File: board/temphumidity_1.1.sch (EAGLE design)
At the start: 33 parts, among them J1 10118192-0001LF, J2 B2B-PH-K-S(LF)(SN), Q1 MMBT2222A, Q2 MMBT2222A, U1 ENS210-LQFM, U2 ESP-WROOM-02, U3 FT231XS-U

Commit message: More revisions on 1.1, added pictures for Readme
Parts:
- removed JP2: (no value), pinhead:PINHD-1X3
- added R15: 4.7k, rcl:R-US_R0805
- added R16: 10k, rcl:R-US_R0805
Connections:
- net 3V3: no longer JP2.1
- net ADC: now also R15.2, R16.1; no longer JP2.2
- net GND: now also R16.2; no longer JP2.3
- net VBAT: now also R15.1
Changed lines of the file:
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@@
 <part name="R9" library="rcl" library_urn="urn:adsk.eagle:library:334" deviceset="R-US_" device="R0805" package3d_urn="urn:adsk.eagle:package:23553/2" value="10k"/>
 <part name="R10" library="rcl" library_urn="urn:adsk.eagle:library:334" deviceset="R-US_" device="R0805" package3d_urn="urn:adsk.eagle:package:23553/2" value="100k"/>
-<part name="JP2" library="pinhead" library_urn="urn:adsk.eagle:library:325" deviceset="PINHD-1X3" device="" package3d_urn="urn:adsk.eagle:package:22458/2"/>
 <part name="J2" library="B2B-PH-K-S_LF__SN_" deviceset="B2B-PH-K-S(LF)(SN)" device=""/>
 <part name="U$2" library="SON50P300X300X80-11N" deviceset="RT9532GQW" device=""/>
@@
 <part name="R14" library="rcl" library_urn="urn:adsk.eagle:library:334" deviceset="R-US_" device="R0805" package3d_urn="urn:adsk.eagle:package:23553/2" value="27"/>
 <part name="VR1" library="AP7366-33W5-7" deviceset="AP7366-33W5-7" device=""/>
+<part name="R15" library="rcl" library_urn="urn:adsk.eagle:library:334" deviceset="R-US_" device="R0805" package3d_urn="urn:adsk.eagle:package:23553/2" value="4.7k"/>
+<part name="R16" library="rcl" library_urn="urn:adsk.eagle:library:334" deviceset="R-US_" device="R0805" package3d_urn="urn:adsk.eagle:package:23553/2" value="10k"/>
 </parts>
 <sheets>
@@
 <attribute name="VALUE" x="24.13" y="-41.402" size="1.778" layer="96"/>
 </instance>
-<instance part="JP2" gate="A" x="-22.86" y="35.56" smashed="yes">
-<attribute name="NAME" x="-29.21" y="41.275" size="1.778" layer="95"/>
-<attribute name="VALUE" x="-29.21" y="27.94" size="1.778" layer="96"/>
-</instance>
 <instance part="VR1" gate="G$1" x="-25.4" y="-50.8" smashed="yes">
 <attribute name="NAME" x="-33.02" y="-44.45" size="2.54" layer="95"/>
 <attribute name="VALUE" x="-33.02" y="-57.15" size="2.54" layer="96" align="top-left"/>
+</instance>
+<instance part="R15" gate="G$1" x="104.14" y="-33.02" smashed="yes" rot="R270">
+<attribute name="NAME" x="105.6386" y="-29.21" size="1.778" layer="95" rot="R270"/>
+<attribute name="VALUE" x="100.838" y="-29.21" size="1.778" layer="96" rot="R270"/>
+</instance>
+<instance part="R16" gate="G$1" x="104.14" y="-48.26" smashed="yes" rot="R270">
+<attribute name="NAME" x="105.6386" y="-44.45" size="1.778" layer="95" rot="R270"/>
+<attribute name="VALUE" x="100.838" y="-44.45" size="1.778" layer="96" rot="R270"/>
 </instance>
 </instances>
@@
 </segment>
 <segment>
-<pinref part="JP2" gate="A" pin="3"/>
-<wire x1="-25.4" y1="33.02" x2="-33.02" y2="33.02" width="0.1524" layer="91"/>
-<label x="-33.02" y="33.02" size="1.778" layer="95" rot="R180"/>
-</segment>
-<segment>
 <pinref part="U2" gate="G$1" pin="GND"/>
 <wire x1="71.12" y1="-63.5" x2="73.66" y2="-63.5" width="0.1524" layer="91"/>
 <label x="73.66" y="-63.5" size="1.778" layer="95"/>
+</segment>
+<segment>
+<pinref part="R16" gate="G$1" pin="2"/>
+<wire x1="104.14" y1="-53.34" x2="104.14" y2="-55.88" width="0.1524" layer="91"/>
+<label x="104.14" y="-55.88" size="1.778" layer="95"/>
 </segment>
 </net>
@@
 <label x="20.32" y="-38.1" size="1.778" layer="95" rot="R180"/>
 </segment>
-<segment>
-<pinref part="JP2" gate="A" pin="1"/>
-<wire x1="-25.4" y1="38.1" x2="-33.02" y2="38.1" width="0.1524" layer="91"/>
-<label x="-33.02" y="38.1" size="1.778" layer="95" rot="R180"/>
-</segment>
 </net>
 <net name="SCL" class="0">
@@
 <wire x1="-58.42" y1="-43.18" x2="-58.42" y2="-40.64" width="0.1524" layer="91"/>
 <label x="-58.42" y="-40.64" size="1.778" layer="95"/>
+</segment>
+<segment>
+<pinref part="R15" gate="G$1" pin="1"/>
+<wire x1="104.14" y1="-27.94" x2="104.14" y2="-25.4" width="0.1524" layer="91"/>
+<label x="104.14" y="-25.4" size="1.778" layer="95"/>
 </segment>
 </net>
@@
 <segment>
 <pinref part="U2" gate="G$1" pin="TOUT"/>
-<wire x1="71.12" y1="-40.64" x2="73.66" y2="-40.64" width="0.1524" layer="91"/>
 <label x="73.66" y="-40.64" size="1.778" layer="95"/>
-</segment>
-<segment>
-<pinref part="JP2" gate="A" pin="2"/>
-<wire x1="-25.4" y1="35.56" x2="-33.02" y2="35.56" width="0.1524" layer="91"/>
-<label x="-33.02" y="35.56" size="1.778" layer="95" rot="R180"/>
-</segment>
-</net>
+<wire x1="71.12" y1="-40.64" x2="104.14" y2="-40.64" width="0.1524" layer="91"/>
+<pinref part="R15" gate="G$1" pin="2"/>
+<wire x1="104.14" y1="-40.64" x2="104.14" y2="-38.1" width="0.1524" layer="91"/>
+<pinref part="R16" gate="G$1" pin="1"/>
+<wire x1="104.14" y1="-40.64" x2="104.14" y2="-43.18" width="0.1524" layer="91"/>
+<junction x="104.14" y="-40.64"/>
+</segment>
+</net>

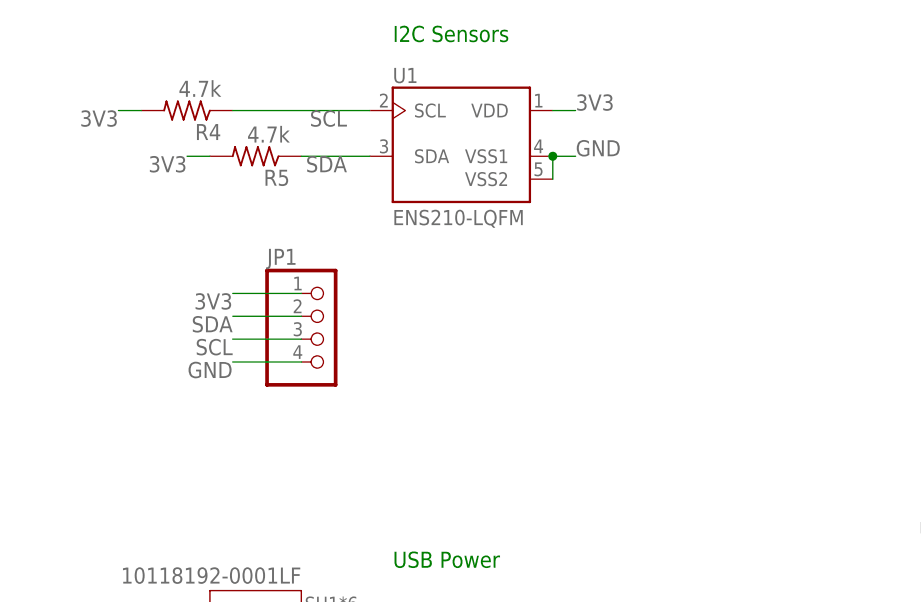
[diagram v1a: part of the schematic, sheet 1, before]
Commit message: Wrote spring application to make use of sql database
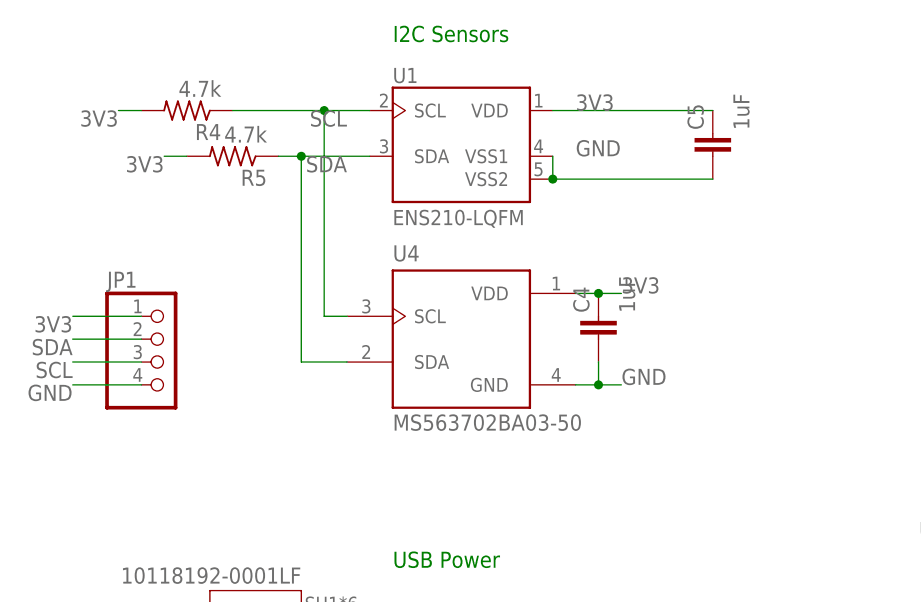
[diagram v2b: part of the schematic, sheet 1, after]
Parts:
- added C4, C5: 1uF, rcl:C-EUC0805
- added U4: MS563702BA03-50, MS563702BA03-50:MS563702BA03-50
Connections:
- net 3V3: now also C4.1, C5.1, U4.VDD
- net GND: now also C4.2, C5.2, U4.GND
- net SCL: now also U4.SCL
- net SDA: now also U4.SDA
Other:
- moved on the sheet: JP1, R5
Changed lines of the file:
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@@
 <part name="R15" library="rcl" library_urn="urn:adsk.eagle:library:334" deviceset="R-US_" device="R0805" package3d_urn="urn:adsk.eagle:package:23553/2" value="4.7k"/>
 <part name="R16" library="rcl" library_urn="urn:adsk.eagle:library:334" deviceset="R-US_" device="R0805" package3d_urn="urn:adsk.eagle:package:23553/2" value="10k"/>
+<part name="U4" library="MS563702BA03-50" deviceset="MS563702BA03-50" device=""/>
+<part name="C4" library="rcl" library_urn="urn:adsk.eagle:library:334" deviceset="C-EU" device="C0805" package3d_urn="urn:adsk.eagle:package:23617/2" value="1uF"/>
+<part name="C5" library="rcl" library_urn="urn:adsk.eagle:library:334" deviceset="C-EU" device="C0805" package3d_urn="urn:adsk.eagle:package:23617/2" value="1uF"/>
 </parts>
 <sheets>
@@
 <attribute name="VALUE" x="-54.61" y="61.722" size="1.778" layer="96" rot="R180"/>
 </instance>
-<instance part="R5" gate="G$1" x="-50.8" y="53.34" smashed="yes" rot="R180">
-<attribute name="NAME" x="-46.99" y="51.8414" size="1.778" layer="95" rot="R180"/>
-<attribute name="VALUE" x="-46.99" y="56.642" size="1.778" layer="96" rot="R180"/>
-</instance>
-<instance part="JP1" gate="A" x="-43.18" y="33.02" smashed="yes">
-<attribute name="NAME" x="-49.53" y="41.275" size="1.778" layer="95"/>
-<attribute name="VALUE" x="-49.53" y="25.4" size="1.778" layer="96"/>
+<instance part="R5" gate="G$1" x="-53.34" y="53.34" smashed="yes" rot="R180">
+<attribute name="NAME" x="-49.53" y="51.8414" size="1.778" layer="95" rot="R180"/>
+<attribute name="VALUE" x="-49.53" y="56.642" size="1.778" layer="96" rot="R180"/>
+</instance>
+<instance part="JP1" gate="A" x="-60.96" y="30.48" smashed="yes">
+<attribute name="NAME" x="-67.31" y="38.735" size="1.778" layer="95"/>
+<attribute name="VALUE" x="-67.31" y="22.86" size="1.778" layer="96"/>
 </instance>
 <instance part="U3" gate="G$1" x="53.34" y="7.62" smashed="yes">
@@
 <attribute name="NAME" x="105.6386" y="-44.45" size="1.778" layer="95" rot="R270"/>
 <attribute name="VALUE" x="100.838" y="-44.45" size="1.778" layer="96" rot="R270"/>
+</instance>
+<instance part="U4" gate="G$1" x="-27.94" y="33.02" smashed="yes">
+<attribute name="NAME" x="-35.566640625" y="41.66351875" size="1.77955" layer="95"/>
+<attribute name="VALUE" x="-35.562240625" y="22.857" size="1.77851875" layer="96"/>
+</instance>
+<instance part="C4" gate="G$1" x="-12.7" y="35.56" smashed="yes">
+<attribute name="NAME" x="-13.716" y="35.941" size="1.778" layer="95" rot="R90"/>
+<attribute name="VALUE" x="-8.636" y="35.941" size="1.778" layer="96" rot="R90"/>
+</instance>
+<instance part="C5" gate="G$1" x="0" y="55.88" smashed="yes">
+<attribute name="NAME" x="-1.016" y="56.261" size="1.778" layer="95" rot="R90"/>
+<attribute name="VALUE" x="4.064" y="56.261" size="1.778" layer="96" rot="R90"/>
 </instance>
 </instances>
@@
 </segment>
 <segment>
+<pinref part="C5" gate="G$1" pin="2"/>
+<wire x1="0" y1="50.8" x2="-17.78" y2="50.8" width="0.1524" layer="91"/>
+<pinref part="U1" gate="G$1" pin="VSS2"/>
 <pinref part="U1" gate="G$1" pin="VSS1"/>
-<pinref part="U1" gate="G$1" pin="VSS2"/>
 <wire x1="-17.78" y1="53.34" x2="-17.78" y2="50.8" width="0.1524" layer="91"/>
-<wire x1="-17.78" y1="53.34" x2="-15.24" y2="53.34" width="0.1524" layer="91"/>
-<junction x="-17.78" y="53.34"/>
 <label x="-15.24" y="53.34" size="1.778" layer="95"/>
+<junction x="-17.78" y="50.8"/>
 </segment>
 <segment>
 <pinref part="JP1" gate="A" pin="4"/>
-<wire x1="-45.72" y1="30.48" x2="-53.34" y2="30.48" width="0.1524" layer="91"/>
-<label x="-53.34" y="30.48" size="1.778" layer="95" rot="R180"/>
+<wire x1="-63.5" y1="27.94" x2="-71.12" y2="27.94" width="0.1524" layer="91"/>
+<label x="-71.12" y="27.94" size="1.778" layer="95" rot="R180"/>
 </segment>
 <segment>
@@
 <wire x1="104.14" y1="-53.34" x2="104.14" y2="-55.88" width="0.1524" layer="91"/>
 <label x="104.14" y="-55.88" size="1.778" layer="95"/>
+</segment>
+<segment>
+<pinref part="U4" gate="G$1" pin="GND"/>
+<wire x1="-15.24" y1="27.94" x2="-12.7" y2="27.94" width="0.1524" layer="91"/>
+<label x="-10.16" y="27.94" size="1.778" layer="95"/>
+<pinref part="C4" gate="G$1" pin="2"/>
+<wire x1="-12.7" y1="27.94" x2="-10.16" y2="27.94" width="0.1524" layer="91"/>
+<wire x1="-12.7" y1="30.48" x2="-12.7" y2="27.94" width="0.1524" layer="91"/>
+<junction x="-12.7" y="27.94"/>
 </segment>
 </net>
@@
 <segment>
 <pinref part="U1" gate="G$1" pin="VDD"/>
-<wire x1="-17.78" y1="58.42" x2="-15.24" y2="58.42" width="0.1524" layer="91"/>
 <label x="-15.24" y="58.42" size="1.778" layer="95"/>
+<pinref part="C5" gate="G$1" pin="1"/>
+<wire x1="-17.78" y1="58.42" x2="0" y2="58.42" width="0.1524" layer="91"/>
 </segment>
 <segment>
 <pinref part="R5" gate="G$1" pin="2"/>
-<wire x1="-55.88" y1="53.34" x2="-58.42" y2="53.34" width="0.1524" layer="91"/>
-<label x="-58.42" y="53.34" size="1.778" layer="95" rot="R180"/>
+<wire x1="-58.42" y1="53.34" x2="-60.96" y2="53.34" width="0.1524" layer="91"/>
+<label x="-60.96" y="53.34" size="1.778" layer="95" rot="R180"/>
 </segment>
 <segment>
@@
 <segment>
 <pinref part="JP1" gate="A" pin="1"/>
-<wire x1="-45.72" y1="38.1" x2="-53.34" y2="38.1" width="0.1524" layer="91"/>
-<label x="-53.34" y="38.1" size="1.778" layer="95" rot="R180"/>
+<wire x1="-63.5" y1="35.56" x2="-71.12" y2="35.56" width="0.1524" layer="91"/>
+<label x="-71.12" y="35.56" size="1.778" layer="95" rot="R180"/>
 </segment>
 <segment>
@@
 <label x="20.32" y="-38.1" size="1.778" layer="95" rot="R180"/>
 </segment>
+<segment>
+<pinref part="U4" gate="G$1" pin="VDD"/>
+<wire x1="-15.24" y1="38.1" x2="-12.7" y2="38.1" width="0.1524" layer="91"/>
+<label x="-10.16" y="38.1" size="1.778" layer="95"/>
+<pinref part="C4" gate="G$1" pin="1"/>
+<wire x1="-12.7" y1="38.1" x2="-10.16" y2="38.1" width="0.1524" layer="91"/>
+<junction x="-12.7" y="38.1"/>
+</segment>
 </net>
 <net name="SCL" class="0">
@@
 <label x="-40.64" y="58.42" size="1.778" layer="95" rot="R180"/>
 <pinref part="R4" gate="G$1" pin="1"/>
-<wire x1="-38.1" y1="58.42" x2="-53.34" y2="58.42" width="0.1524" layer="91"/>
+<wire x1="-38.1" y1="58.42" x2="-43.18" y2="58.42" width="0.1524" layer="91"/>
+<pinref part="U4" gate="G$1" pin="SCL"/>
+<wire x1="-43.18" y1="58.42" x2="-53.34" y2="58.42" width="0.1524" layer="91"/>
+<wire x1="-40.64" y1="35.56" x2="-43.18" y2="35.56" width="0.1524" layer="91"/>
+<wire x1="-43.18" y1="35.56" x2="-43.18" y2="58.42" width="0.1524" layer="91"/>
+<junction x="-43.18" y="58.42"/>
 </segment>
 <segment>
 <pinref part="JP1" gate="A" pin="3"/>
-<wire x1="-45.72" y1="33.02" x2="-53.34" y2="33.02" width="0.1524" layer="91"/>
-<label x="-53.34" y="33.02" size="1.778" layer="95" rot="R180"/>
+<wire x1="-63.5" y1="30.48" x2="-71.12" y2="30.48" width="0.1524" layer="91"/>
+<label x="-71.12" y="30.48" size="1.778" layer="95" rot="R180"/>
 </segment>
 </net>
@@
 <pinref part="R5" gate="G$1" pin="1"/>
 <wire x1="-38.1" y1="53.34" x2="-45.72" y2="53.34" width="0.1524" layer="91"/>
+<pinref part="U4" gate="G$1" pin="SDA"/>
+<wire x1="-45.72" y1="53.34" x2="-48.26" y2="53.34" width="0.1524" layer="91"/>
+<wire x1="-40.64" y1="30.48" x2="-45.72" y2="30.48" width="0.1524" layer="91"/>
+<wire x1="-45.72" y1="30.48" x2="-45.72" y2="53.34" width="0.1524" layer="91"/>
+<junction x="-45.72" y="53.34"/>
 </segment>
 <segment>
 <pinref part="JP1" gate="A" pin="2"/>
-<wire x1="-45.72" y1="35.56" x2="-53.34" y2="35.56" width="0.1524" layer="91"/>
-<label x="-53.34" y="35.56" size="1.778" layer="95" rot="R180"/>
-</segment>
-</net>
+<wire x1="-63.5" y1="33.02" x2="-71.12" y2="33.02" width="0.1524" layer="91"/>
+<label x="-71.12" y="33.02" size="1.778" layer="95" rot="R180"/>
+</segment>
+</net>

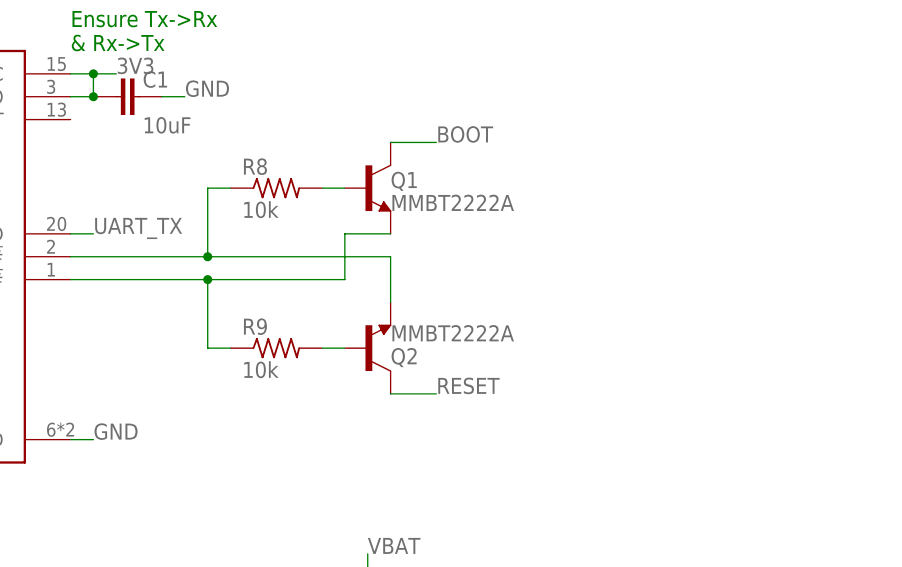
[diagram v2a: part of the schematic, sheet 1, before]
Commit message: Added breakout so old programmers can program new boards
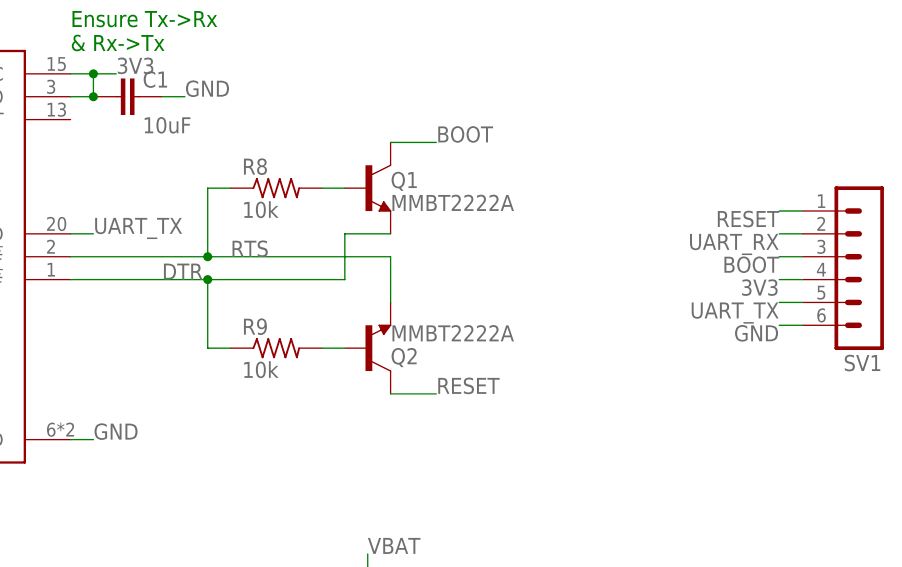
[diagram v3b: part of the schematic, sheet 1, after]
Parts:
- added SV1: (no value), con-lstb:MA06-1
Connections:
- net N$4 renamed RTS
- net N$6 renamed DTR
- net 3V3: now also SV1.4
- net BOOT: now also SV1.3
- net GND: now also SV1.6
- net RESET: now also SV1.1
- net UART_RX: now also SV1.2
- net UART_TX: now also SV1.5
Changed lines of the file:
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@@
 <part name="C4" library="rcl" library_urn="urn:adsk.eagle:library:334" deviceset="C-EU" device="C0805" package3d_urn="urn:adsk.eagle:package:23617/2" value="1uF"/>
 <part name="C5" library="rcl" library_urn="urn:adsk.eagle:library:334" deviceset="C-EU" device="C0805" package3d_urn="urn:adsk.eagle:package:23617/2" value="1uF"/>
+<part name="SV1" library="con-lstb" library_urn="urn:adsk.eagle:library:162" deviceset="MA06-1" device="" package3d_urn="urn:adsk.eagle:package:8340/1"/>
 </parts>
 <sheets>
@@
 <attribute name="VALUE" x="4.064" y="56.261" size="1.778" layer="96" rot="R90"/>
 </instance>
+<instance part="SV1" gate="1" x="160.02" y="5.08" smashed="yes" rot="R180">
+<attribute name="VALUE" x="161.29" y="17.78" size="1.778" layer="96" rot="R180"/>
+<attribute name="NAME" x="161.29" y="-3.302" size="1.778" layer="95" rot="R180"/>
+</instance>
 </instances>
 <busses>
@@
 <junction x="-12.7" y="27.94"/>
 </segment>
+<segment>
+<pinref part="SV1" gate="1" pin="6"/>
+<wire x1="152.4" y1="0" x2="149.86" y2="0" width="0.1524" layer="91"/>
+<label x="149.86" y="0" size="1.778" layer="95" rot="R180"/>
+</segment>
 </net>
 <net name="N$1" class="0">
@@
 <junction x="-12.7" y="38.1"/>
 </segment>
+<segment>
+<pinref part="SV1" gate="1" pin="4"/>
+<wire x1="152.4" y1="5.08" x2="149.86" y2="5.08" width="0.1524" layer="91"/>
+<label x="149.86" y="5.08" size="1.778" layer="95" rot="R180"/>
+</segment>
 </net>
 <net name="SCL" class="0">
@@
 </segment>
 </net>
-<net name="N$4" class="0">
+<net name="RTS" class="0">
 <segment>
 <pinref part="U3" gate="G$1" pin="!RTS#"/>
@@
 <pinref part="R8" gate="G$1" pin="1"/>
 <wire x1="86.36" y1="15.24" x2="88.9" y2="15.24" width="0.1524" layer="91"/>
-</segment>
-</net>
-<net name="N$6" class="0">
+<label x="88.9" y="7.62" size="1.778" layer="95"/>
+</segment>
+</net>
+<net name="DTR" class="0">
 <segment>
 <pinref part="U3" gate="G$1" pin="!DTR#"/>
@@
 <pinref part="R9" gate="G$1" pin="1"/>
 <wire x1="86.36" y1="-2.54" x2="88.9" y2="-2.54" width="0.1524" layer="91"/>
+<label x="81.28" y="5.08" size="1.778" layer="95"/>
 </segment>
 </net>
@@
 <label x="33.02" y="-58.42" size="1.778" layer="95" rot="R180"/>
 </segment>
+<segment>
+<pinref part="SV1" gate="1" pin="2"/>
+<wire x1="152.4" y1="10.16" x2="149.86" y2="10.16" width="0.1524" layer="91"/>
+<label x="149.86" y="10.16" size="1.778" layer="95" rot="R180"/>
+</segment>
 </net>
 <net name="UART_TX" class="0">
@@
 <label x="33.02" y="-60.96" size="1.778" layer="95" rot="R180"/>
 </segment>
+<segment>
+<pinref part="SV1" gate="1" pin="5"/>
+<wire x1="152.4" y1="2.54" x2="149.86" y2="2.54" width="0.1524" layer="91"/>
+<label x="149.86" y="2.54" size="1.778" layer="95" rot="R180"/>
+</segment>
 </net>
 <net name="N$9" class="0">
@@
 <label x="33.02" y="-45.72" size="1.778" layer="95" rot="R180"/>
 </segment>
+<segment>
+<pinref part="SV1" gate="1" pin="3"/>
+<wire x1="152.4" y1="7.62" x2="149.86" y2="7.62" width="0.1524" layer="91"/>
+<label x="149.86" y="7.62" size="1.778" layer="95" rot="R180"/>
+</segment>
 </net>
 <net name="RESET" class="0">
@@
 <label x="73.66" y="-38.1" size="1.778" layer="95"/>
 </segment>
-</net>
+<segment>
+<pinref part="SV1" gate="1" pin="1"/>
+<wire x1="152.4" y1="12.7" x2="149.86" y2="12.7" width="0.1524" layer="91"/>
+<label x="149.86" y="12.7" size="1.778" layer="95" rot="R180"/>
+</segment>
+</net>
